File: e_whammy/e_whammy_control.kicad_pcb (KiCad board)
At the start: 2 copper layers, 34 x 14 mm, 35 parts, among them J1 Conn_01x03, J2 Conn_01x03, J3 Conn_01x02, J4 Conn_01x02, U2 HT7550-1, U3 TLV9004IPWR

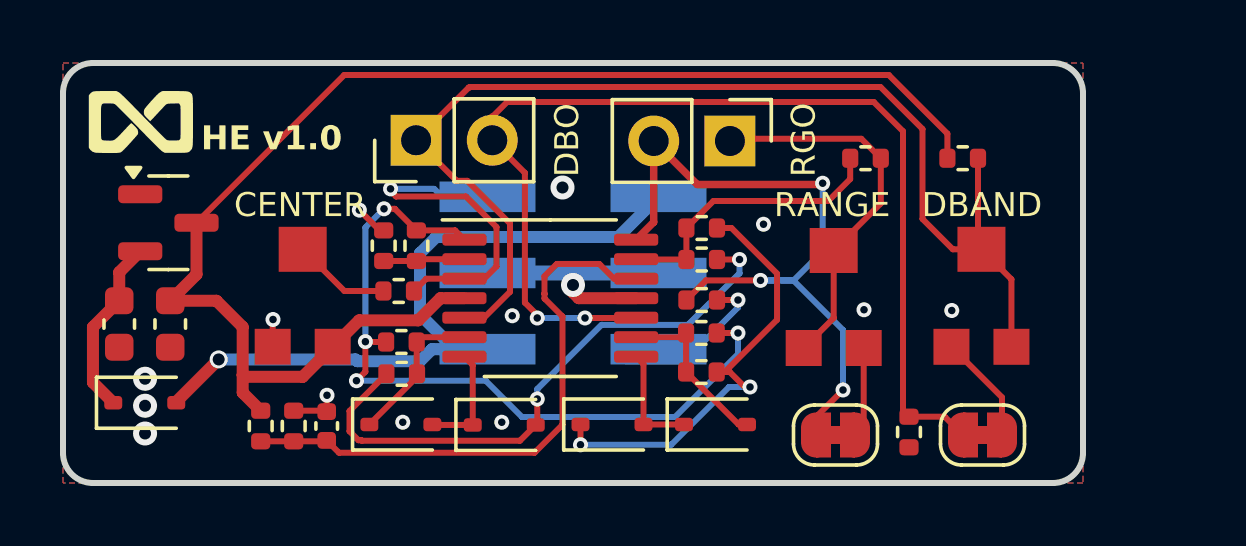
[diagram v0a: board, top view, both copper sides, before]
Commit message: E-Whammy update: bug fixes and refinements
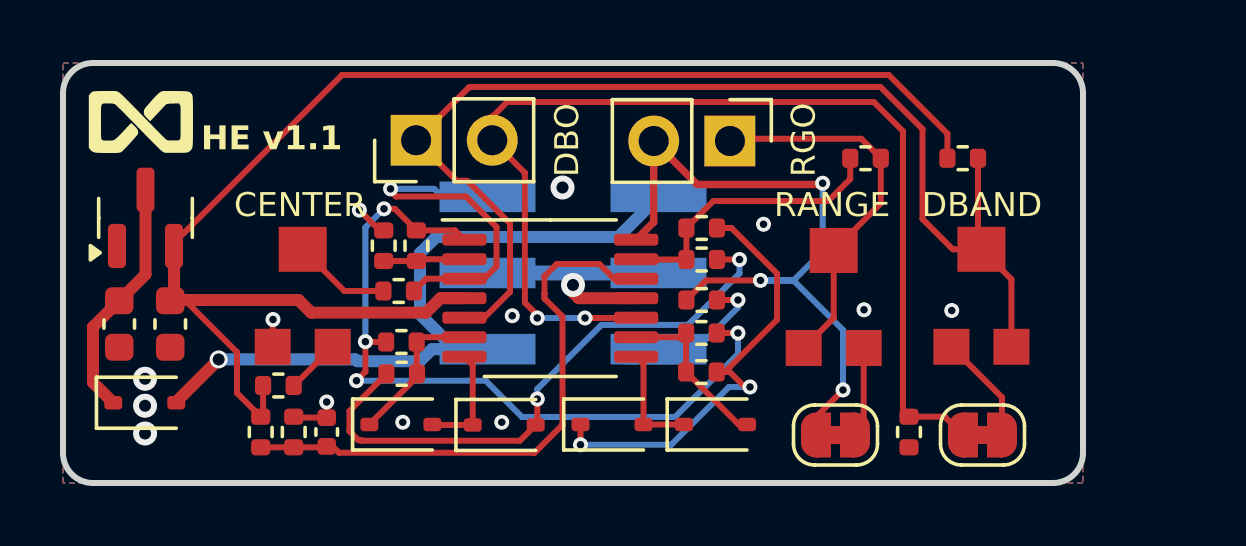
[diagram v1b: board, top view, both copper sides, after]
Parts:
- added R4: 47K, Resistor_SMD:R_0402_1005Metric, F.Cu at (142.2, 149.8)
- U2: footprint Package_TO_SOT_SMD:SOT-23 -> cycfi_library:SOT-23-132
- moved U2 0.78 mm to (137.8, 144.2), turned to 90 degrees
- moved C1 0.20 mm to (143.8, 151.3)
- moved R15 0.20 mm to (141.6, 151.3)
- moved R16 0.20 mm to (142.7, 151.3)
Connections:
- RV1 pad 3: 5v -> Net-(R4-Pad1)
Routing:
- net 5v: track 46.0 -> 48.4 mm
- net Net-(D2-K): track 5.98 -> 8.11 mm
- net Net-(R4-Pad1): track 0.00 -> 1.83 mm
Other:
- board text added: "HE v1.1"
- board text removed: "HE v1.0"

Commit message: Updated 1-3-2 pinout
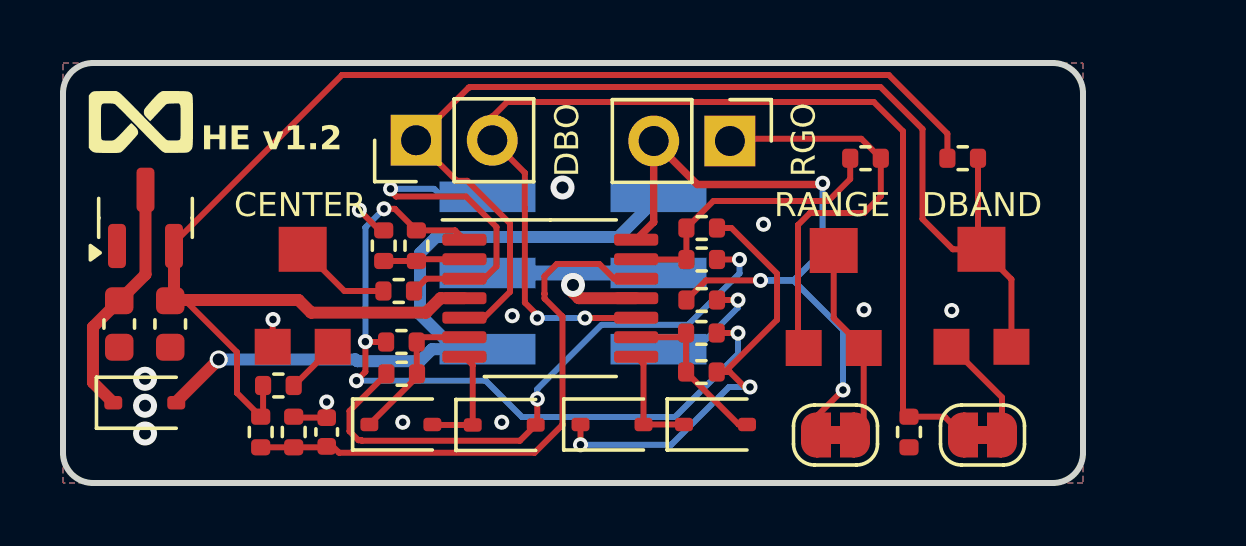
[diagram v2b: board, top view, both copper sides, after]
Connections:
- RV2 pad 2: /RO1 -> Net-(JP2-B)
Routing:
- net Net-(JP2-B): track 3.10 -> 6.77 mm
- net /RO1: track 12.7 -> 13.9 mm
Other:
- board text added: "HE v1.2"
- board text removed: "HE v1.1"
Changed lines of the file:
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@@
 			(size 1.6 1.5)
 			(layers "F.Cu" "F.Mask" "F.Paste")
-			(net 16 "/RO1")
+			(net 23 "Net-(JP2-B)")
 			(pinfunction "2")
 			(pintype "passive")
@@
 		)
 	)
-	(gr_text "HE v1.1"
+	(gr_text "HE v1.2"
 		(at 139.6 141.975 0)
 		(layer "F.SilkS")
@@
 	)
 	(segment
-		(start 162.26 142.175)
-		(end 162.26 143.68)
-		(width 0.2)
-		(layer "F.Cu")
-		(net 16)
-	)
-	(segment
-		(start 162.26 143.68)
-		(end 160.69 145.25)
+		(start 161.699 144.001)
+		(end 162.26 143.44)
 		(width 0.2)
 		(layer "F.Cu")
@@
 	)
 	(segment
-		(start 160.69 145.25)
-		(end 160.69 147.5)
+		(start 162.26 143.44)
+		(end 162.26 142.175)
 		(width 0.2)
 		(layer "F.Cu")
@@
 	)
 	(segment
-		(start 160.69 147.5)
-		(end 159.69 148.5)
+		(start 159.5 148.31)
+		(end 159.5 144.4)
+		(width 0.2)
+		(layer "F.Cu")
+		(net 16)
+	)
+	(segment
+		(start 159.899 144.001)
+		(end 161.699 144.001)
+		(width 0.2)
+		(layer "F.Cu")
+		(net 16)
+	)
+	(segment
+		(start 159.5 144.4)
+		(end 159.899 144.001)
+		(width 0.2)
+		(layer "F.Cu")
+		(net 16)
+	)
+	(segment
+		(start 159.69 148.5)
+		(end 159.5 148.31)
 		(width 0.2)
 		(layer "F.Cu")
@@
 	)
 	(segment
+		(start 160.69 147.5)
+		(end 161.69 148.5)
+		(width 0.2)
+		(layer "F.Cu")
+		(net 23)
+	)
+	(segment
 		(start 161.75 148.44)
 		(end 161.69 148.5)
@@
 		(width 0.2)
 		(layer "F.Cu")
+		(net 23)
+	)
+	(segment
+		(start 160.69 145.25)
+		(end 160.69 147.5)
+		(width 0.2)
+		(layer "F.Cu")

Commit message: Added signal shunt with HP filter (DC blocking) to allow fine vibrato within the deadband.
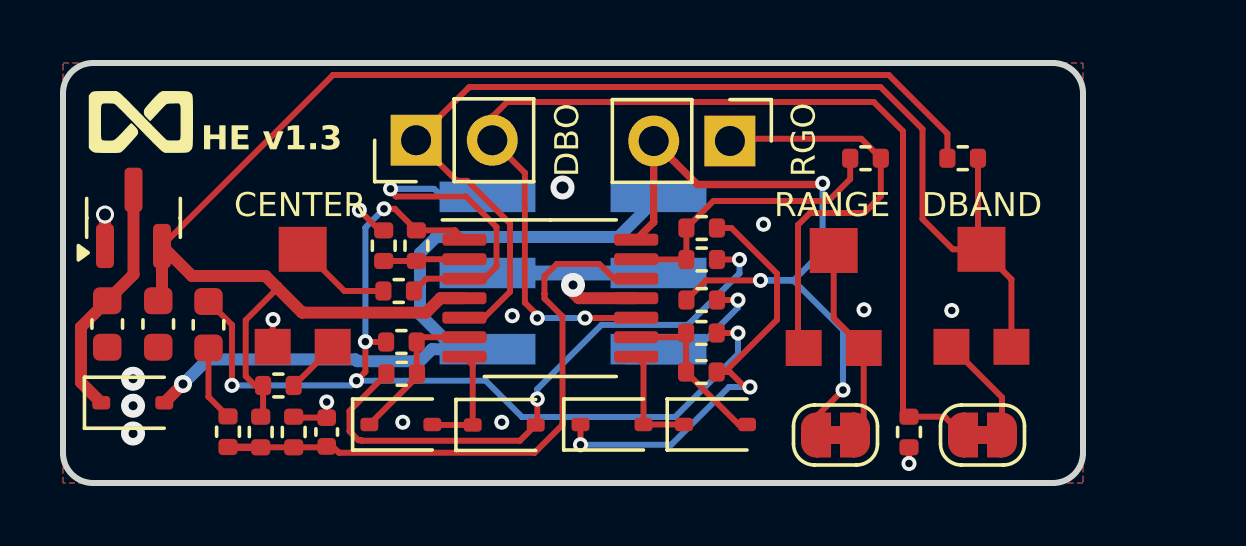
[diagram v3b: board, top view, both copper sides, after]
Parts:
- added C2: 10uF, Capacitor_SMD:C_0603_1608Metric, F.Cu at (139.8, 147.7)
- added R17: 10K, Resistor_SMD:R_0402_1005Metric, F.Cu at (140.5, 151.3)
- C1: value 100nF -> 1uF
- moved C3 0.40 mm to (136.5, 147.7)
- moved D2 0.40 mm to (137.3, 150.3)
- moved U2 0.40 mm to (137.3, 144.2)
- moved C4 0.40 mm to (138.2, 147.7)
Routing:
- net /PRE: track 25.4 -> 32.7 mm, vias 4 -> 5
- net Net-(C2-Pad2): track 0.00 -> 2.55 mm
- net GND: track 11.8 -> 13.4 mm, vias 14 -> 16
- net /VREF: track 19.2 -> 20.3 mm
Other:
- board text added: "HE v1.3"
- board text removed: "HE v1.2"

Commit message: - Added a precision voltage reference for VREF - Removed deadband bypass
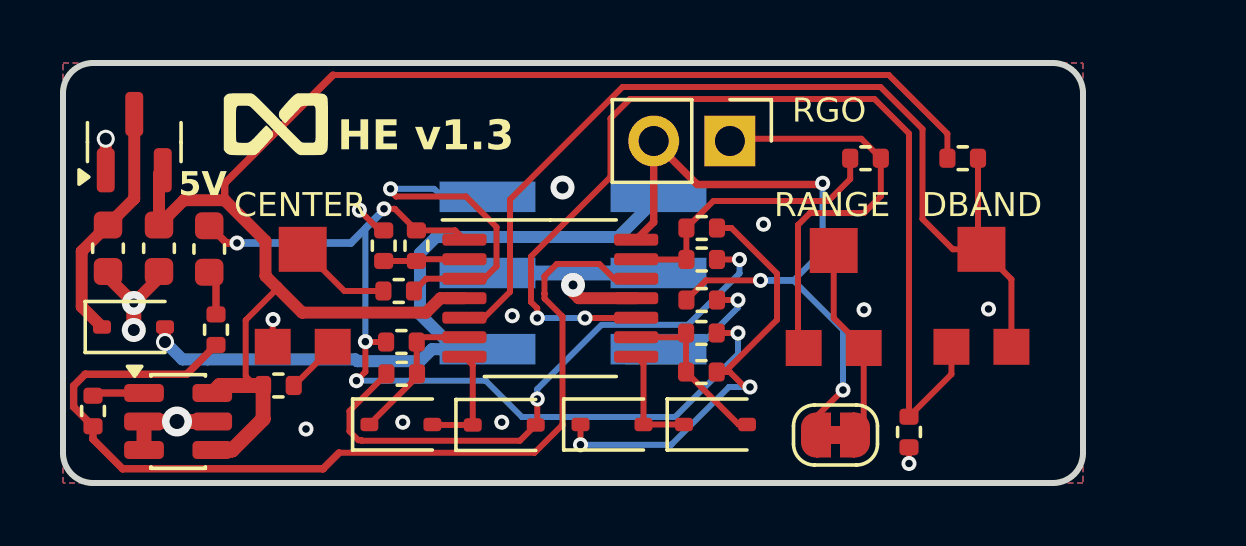
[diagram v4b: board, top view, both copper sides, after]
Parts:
- removed C1: 1uF, Capacitor_SMD:C_0402_1005Metric
- removed J3: Conn_01x02, Connector_PinHeader_2.54mm:PinHeader_1x02_P2.54mm_Vertical
- removed JP1: SolderJumper_2_Bridged, Jumper:SolderJumper-2_P1.3mm_Bridged_RoundedPad1.0x1.5mm
- removed R16: 10K, Resistor_SMD:R_0402_1005Metric
- added U1: MCP1501T-25E/CHY, Package_TO_SOT_SMD:SOT-23-6, F.Cu at (138.8, 150.9)
- C2: value 10uF -> 2.2uF
- R15: value 10K -> 4.7K
- moved R15 5.63 mm to (136.0, 150.6), turned to -90 degrees
- moved G*** 4.50 mm to (142.1, 141.1)
- moved R17 3.42 mm to (140.1, 147.9)
- moved C2 2.53 mm to (139.9, 145.2)
- moved U2 2.53 mm to (137.4, 141.6)
- moved C3 2.53 mm to (136.5, 145.2)
- moved D2 2.53 mm to (137.3, 147.8)
- moved C4 2.53 mm to (138.2, 145.2)
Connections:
- R15 pad 1: /VREF -> VREF
- R15 pad 2: 5v -> Net-(U3D-+)
- R17 pad 2: /VREF -> Net-(U3D-+)
- RV3 pad 1: Net-(JP1-B) -> /DLO
- U3 pad 12: /VREF -> Net-(U3D-+)
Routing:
- net Net-(U3D-+): track 0.00 -> 32.7 mm
- net /VREF: track 20.3 -> 0.00 mm
- net /DHI: track 38.7 -> 33.0 mm
- net GND: track 13.4 -> 18.7 mm
- net Net-(JP1-B): track 3.64 -> 0.00 mm
- net 5v: track 48.3 -> 51.8 mm
- net /DLO: track 36.6 -> 34.2 mm
- net VREF: track 0.00 -> 1.74 mm
- net Net-(C2-Pad2): track 2.55 -> 1.50 mm
- net /PRE: track 32.7 -> 32.0 mm
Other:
- board text added: "5V"
- board text removed: "DBO"

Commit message: New v2 eWhammy control scheme using differentiator and switched auto-centering integrator
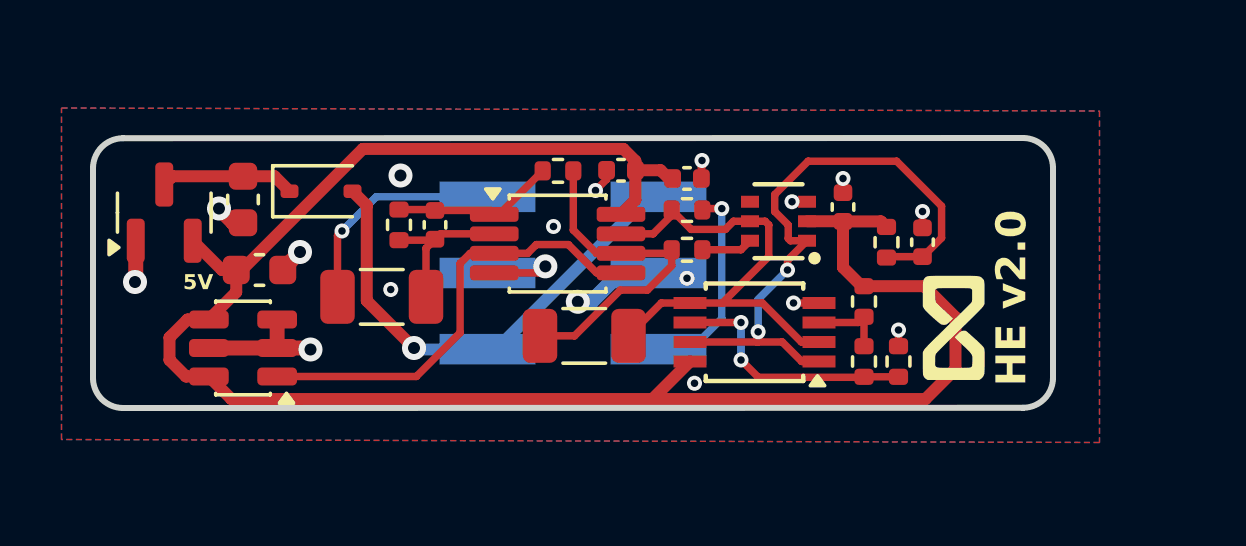
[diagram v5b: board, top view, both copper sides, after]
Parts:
- removed D2, D3, D4, D5: 1N4148WS, Diode_SMD:D_SOD-323
- removed J4: Conn_01x02, Connector_PinHeader_2.54mm:PinHeader_1x02_P2.54mm_Vertical
- removed JP2: SolderJumper_2_Bridged, Jumper:SolderJumper-2_P1.3mm_Bridged_RoundedPad1.0x1.5mm
- removed R10, R11, R12, R13, R14, R17: 10K, Resistor_SMD:R_0402_1005Metric
- removed R15: 4.7K, Resistor_SMD:R_0402_1005Metric
- removed R9: 100K, Resistor_SMD:R_0402_1005Metric
- removed RV1, RV3: 10K, cycfi_library:TC33X-2
- removed RV2: 100K, cycfi_library:TC33X-2
- added C1: 10uF, Capacitor_SMD:C_0603_1608Metric, F.Cu at (141.0, 143.6)
- added C5: 100nF, Capacitor_SMD:C_0402_1005Metric, F.Cu at (161.0, 143.8)
- added C6: 100nF (COG), Capacitor_SMD:C_1206_3216Metric, F.Cu at (145.6, 146.8)
- added C7: 1nF (COG), Capacitor_SMD:C_0402_1005Metric, F.Cu at (147.4, 144.4)
- added C8: 100nF, Capacitor_SMD:C_0402_1005Metric, F.Cu at (163.7, 145.0)
- added C9: 100nF (COG), Capacitor_SMD:C_1206_3216Metric, F.Cu at (152.4, 148.1)
- added U4: ADG779, cycfi_library:KS_6_ADI, F.Cu at (158.8, 144.3)
- added U5: LM393PWR, Package_SO:TSSOP-8_3x3mm_P0.65mm, F.Cu at (158.1, 148.0)
- C2: value 2.2uF -> 10uF
- C3, C4: value 10uF -> 100nF; footprint Capacitor_SMD:C_0603_1608Metric -> Capacitor_SMD:C_0402_1005Metric
- R1, R3: value 10K -> 120k
- R2, R5: value 10K -> 10k
- R4: value 47K -> 10M
- R6: value 47K -> 100k
- R7: value 1K -> 2M
- R8: value 100K -> 1K
- U3: value TLV9004IPWR -> TLV9002IDGKR; footprint cycfi_library:TSSOP-14_4.4x5mm_P0.65mm -> Package_SO:VSSOP-8_3x3mm_P0.65mm
- moved G*** 23.6 mm to (164.7, 147.8), turned to 90 degrees
- moved C3 19.4 mm to (155.8, 142.8), turned to 180 degrees
- moved R3 16.6 mm to (162.8, 148.9), turned to -90 degrees
- moved R1 16.1 mm to (161.7, 146.9), turned to 90 degrees
- moved C4 15.6 mm to (153.6, 142.6), turned to 0 degrees
- moved R2 15.4 mm to (161.7, 148.9)
- moved D1 9.90 mm to (143.6, 143.3)
- moved R8 9.35 mm to (155.8, 143.9), turned to 0 degrees
- moved R5 6.87 mm to (162.4, 145.0), turned to 90 degrees
- moved R4 6.70 mm to (146.2, 144.4), turned to 90 degrees
- moved R6 6.65 mm to (151.5, 142.6)
- moved U1 3.27 mm to (141.0, 148.5), turned to 180 degrees
- moved U2 2.55 mm to (138.4, 144.0)
- moved U3 1.84 mm to (151.5, 145.0)
- moved C2 1.82 mm to (141.6, 145.9), turned to 0 degrees
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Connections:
- C2 pad 1: /PRE -> 5v
- C2 pad 2: Net-(C2-Pad2) -> GND
- C3 pad 1: Net-(D2-K) -> GND
- C3 pad 2: GND -> 5v
- C4 pad 1: 5v -> GND
- C4 pad 2: GND -> 5v
- D1 pad 2: /PR -> V+
- R1 pad 1: GND -> Net-(U5A-+)
- R1 pad 2: Net-(U3A--) -> 5v
- R2 pad 1: Net-(U3A--) -> Net-(U5B--)
- R2 pad 2: /PRE -> Net-(U5A-+)
- R3 pad 1: /PRE -> GND
- R3 pad 2: Net-(D3-K) -> Net-(U5B--)
- R4 pad 1: Net-(R4-Pad1) -> Net-(U3A--)
- R4 pad 2: 5v -> Net-(C7-Pad2)
- R5 pad 1: /PRE -> Net-(C8-Pad2)
- R5 pad 2: Net-(D5-A) -> 5v
- R6 pad 1: Net-(R6-Pad1) -> Net-(C7-Pad2)
- R6 pad 2: HE_SENSOR -> Net-(U3B--)
- R7 pad 1: /RO2 -> Net-(U3B--)
- R7 pad 2: OUT -> RESET
- R8 pad 1: /DHI -> INTEG_OUT
- R8 pad 2: 5v -> OUT
- U2 pad 2: Net-(D2-K) -> Net-(D1-K)
- U3 pad 1: /PRE -> Net-(C7-Pad2)
- U3 pad 3: HE_SENSOR -> VREF
- U3 pad 4: 5v -> GND
- U3 pad 5: /DHI -> VREF
- U3 pad 6: Net-(D3-K) -> Net-(U3B--)
- U3 pad 7: Net-(D1-K) -> INTEG_OUT
- U3 pad 8: Net-(D4-A) -> 5v
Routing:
- net /DLO: track 34.2 -> 0.00 mm, vias 2 -> 0
- net /DHI: track 33.0 -> 0.00 mm
- net Net-(U3D-+): track 32.7 -> 0.00 mm
- net /PRE: track 32.0 -> 0.00 mm, vias 5 -> 0
- net /RO2: track 24.6 -> 0.00 mm, vias 3 -> 0
- net Net-(C8-Pad2): track 0.00 -> 20.7 mm, vias 0 -> 2
- net /PR: track 19.7 -> 0.00 mm, vias 2 -> 0
- net INTEG_OUT: track 0.00 -> 16.4 mm
- net /NR: track 15.3 -> 0.00 mm, vias 2 -> 0
- net /RO1: track 13.9 -> 0.00 mm
- net VREF: track 1.74 -> 15.0 mm
- net 5v: track 51.8 -> 64.0 mm
- net Net-(U3B--): track 0.00 -> 11.5 mm
- net Net-(U3D--): track 9.56 -> 0.00 mm
- net V+: track 25.2 -> 16.4 mm
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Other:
- board size 34 x 14 mm -> 32 x 9 mm
- board text added: "HE v2.0"
- board text removed: "CENTER"
- board text removed: "DBAND"
- board text removed: "HE v1.3"
- board text removed: "HE-SENSOR"
- board text removed: "OUTPUT"
- board text removed: "RANGE"
- board text removed: "RGO"

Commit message: - Center the outline - Adjust width to 10 mm (min. JLCPCB allowed)
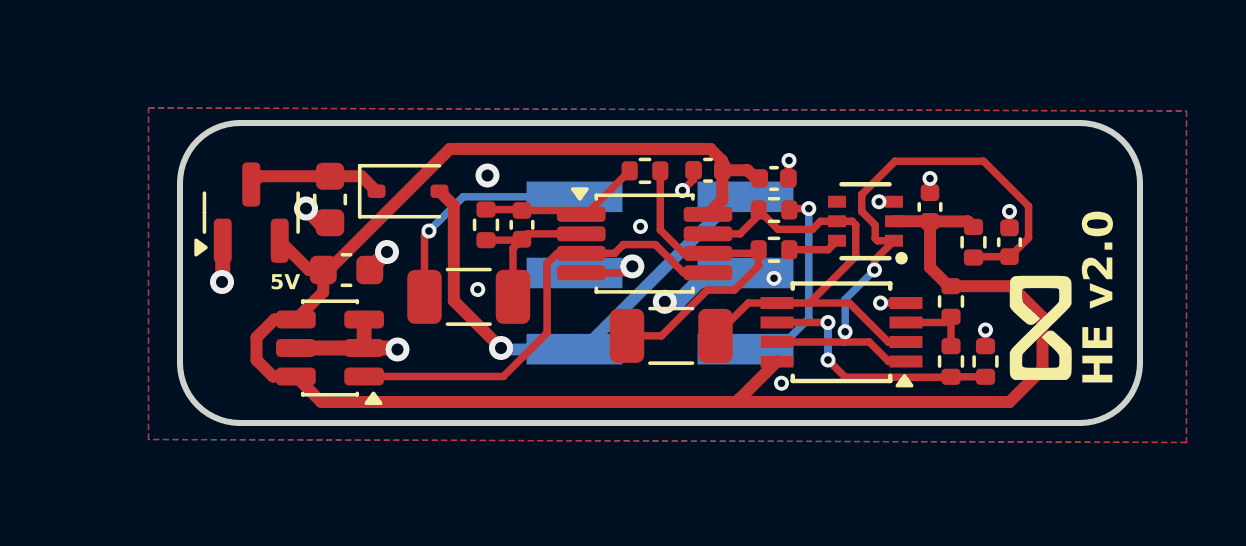
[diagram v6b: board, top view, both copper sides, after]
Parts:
- moved C1 2.90 mm to (143.9, 143.6)
- moved C4 2.90 mm to (156.5, 142.6)
- moved C5 2.90 mm to (163.9, 143.8)
- moved C6 2.90 mm to (148.5, 146.8)
- moved C7 2.90 mm to (150.3, 144.4)
- moved C8 2.90 mm to (166.6, 145.0)
- moved C9 2.90 mm to (155.3, 148.1)
- moved D1 2.90 mm to (146.5, 143.3)
- moved G*** 2.90 mm to (167.6, 147.8)
- moved J1 2.90 mm to (152.1, 146.0)
- moved J2 2.90 mm to (157.8, 146.0)
- moved R1 2.90 mm to (164.6, 146.9)
- moved R2 2.90 mm to (164.6, 148.9)
- moved R3 2.90 mm to (165.8, 148.9)
- moved R4 2.90 mm to (149.1, 144.4)
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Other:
- board size 32 x 9 mm -> 32 x 10 mm

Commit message: (ewhammy v2) - Component fixes - Added test points
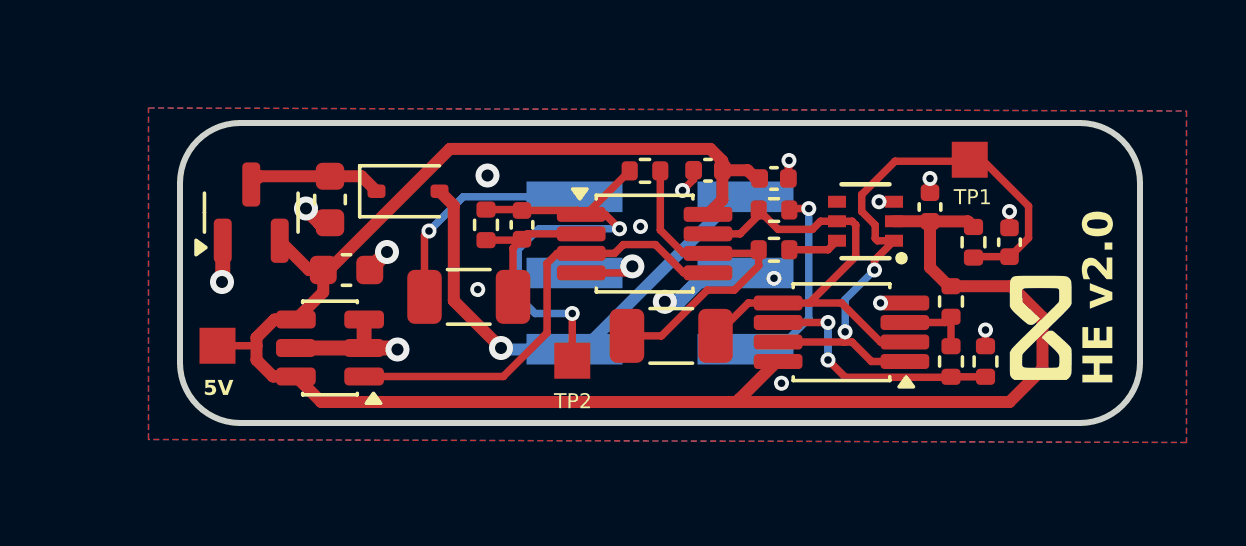
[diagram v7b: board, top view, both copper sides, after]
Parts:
- added TP1: TestPoint, cycfi_library:single-pad-1.2x1.2, F.Cu at (165.2, 142.2)
- added TP2: TestPoint, cycfi_library:single-pad-1.2x1.2, F.Cu at (152.0, 148.9)
- added TP3: TestPoint, cycfi_library:single-pad-1.2x1.2, F.Cu at (140.2, 148.4)
- U5: value LM393PWR -> LM393BIDGKR; footprint Package_SO:TSSOP-8_3x3mm_P0.65mm -> Package_SO:VSSOP-8_3x3mm_P0.65mm
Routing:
- net Net-(C7-Pad2): track 5.46 -> 15.8 mm, vias 0 -> 2
- net 5v: track 64.2 -> 65.5 mm
